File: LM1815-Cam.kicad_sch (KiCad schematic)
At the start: 13 parts, among them IC2A1 LM1815MX_NOPB

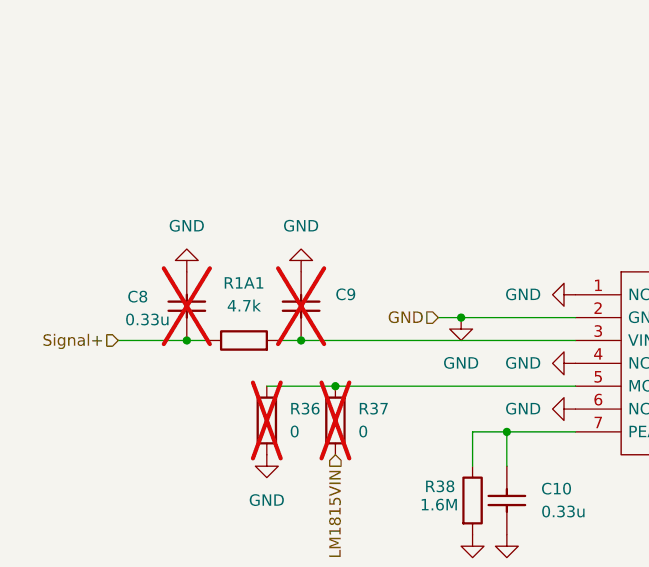
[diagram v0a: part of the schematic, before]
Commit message: Fixed mismatch between part designators?
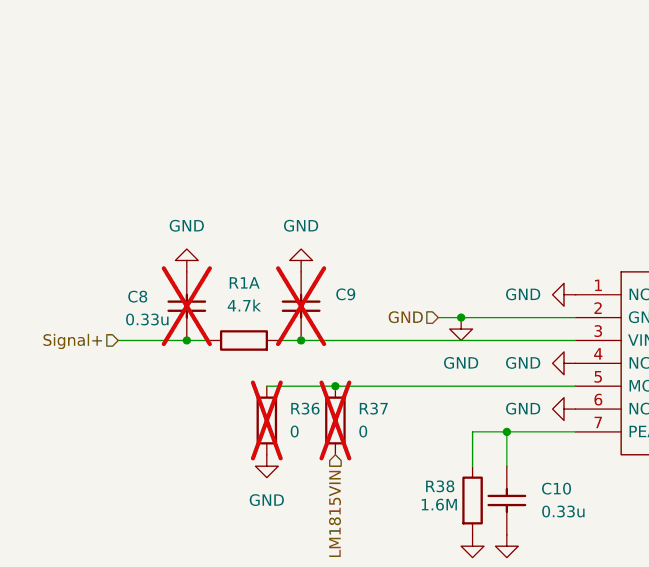
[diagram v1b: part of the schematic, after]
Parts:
- renumbered R1A1 to R1A
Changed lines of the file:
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@@
 		(dnp no)
 		(fields_autoplaced yes)
-		(property "Reference" "R1A1"
+		(property "Reference" "R1A"
 			(at 39.37 53.34 90)
 			(effects
@@
 			(project "VFRECU-VR"
 				(path "/90b72e19-92bc-40db-bd4d-f17fb5de93ea/6c826ae6-85e5-4f50-9882-510a117c9583"
-					(reference "R1A1")
+					(reference "R1A")
 					(unit 1)
 				)
